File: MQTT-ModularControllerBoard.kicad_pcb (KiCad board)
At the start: 4 copper layers, 200 x 45 mm, 83 parts, among them IC301 LM74700QDBVTQ1, IC401 TLV76733DRVR, IC403 LM74700QDBVTQ1, J301 1715721, J501 A2541HWV-10P, J502 A2541HWV-10P, J503 A2541HWV-10P, J504 A2541HWV-10P, J505 A2541HWV-10P, J506 A2541HWV-10P, J507 A2541HWV-10P, J508 A2541HWV-10P, J601 1051640001, Q301 60V 38A, Q402 60V 38A, U201 ESP32-S3-WROOM-1U-N16R8, U601 ESD Protection IC

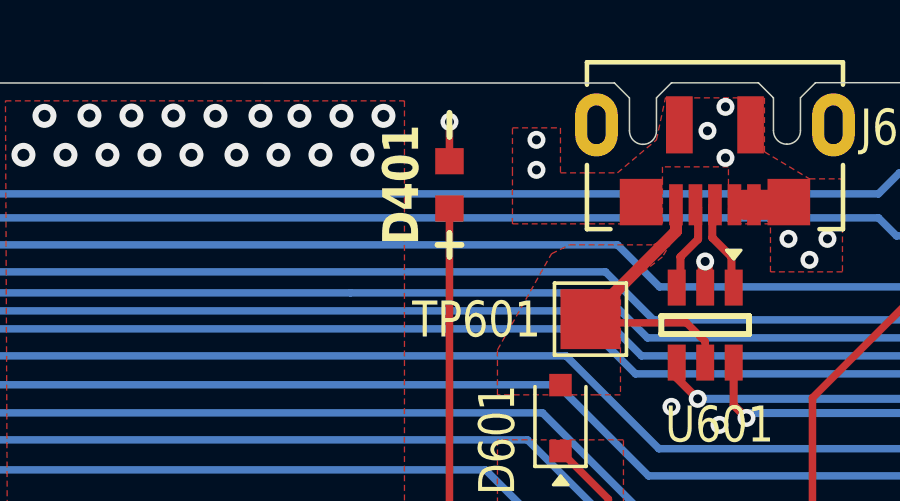
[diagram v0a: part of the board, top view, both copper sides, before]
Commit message: Silkscreen Updates and BOM added
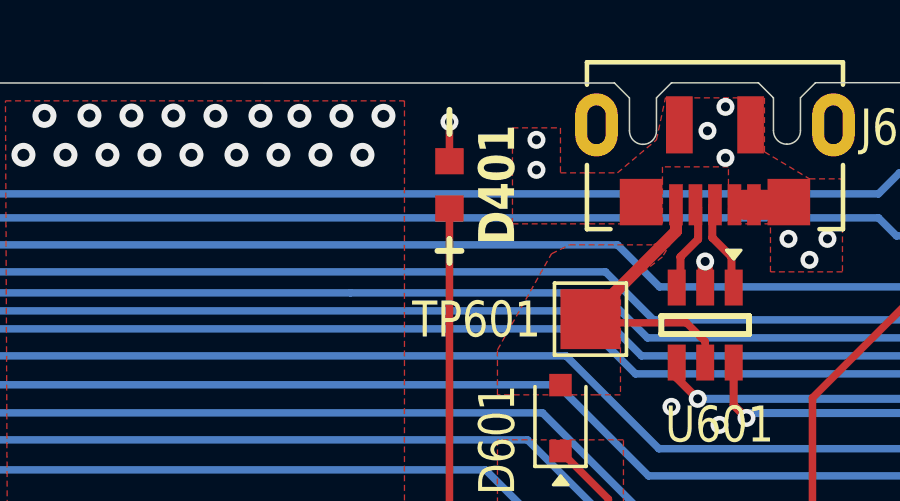
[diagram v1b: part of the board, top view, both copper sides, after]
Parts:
- turned D401 to 90 degrees
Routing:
- net Net-(D401-A): track 20.7 -> 22.0 mm
- net GND: track 78.1 -> 76.8 mm
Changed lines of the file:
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@@
 	(footprint "JLCPCB Basic:LED_0603_1608Metric"
 		(layer "F.Cu")
-		(at 171.5 94.9 -90)
+		(at 171.5 94.9 90)
 		(descr "LED SMD 0603 (1608 Metric), square (rectangular) end terminal, IPC-7351 nominal, (Body size source: http://www.tortai-tech.com/upload/download/2011102023233369053.pdf), generated with kicad-footprint-generator")
 		(tags "LED")
 		(property "Reference" "D401"
-			(at 0 1.6 270)
+			(at 0 1.6 90)
 			(layer "F.SilkS")
 			(effects
@@
 		)
 		(property "Value" "KT-0603R"
-			(at 4.1 7.4 180)
+			(at 4.1 7.4 0)
 			(layer "F.Fab")
 			(hide yes)
@@
 		)
 		(property "Sim.Pins" "1=K 2=A"
-			(at 0 0 270)
+			(at 0 0 90)
 			(unlocked yes)
 			(layer "F.Fab")
@@
 		)
 		(property "Manufacturer" "Hubei KENTO Elec"
-			(at 0 0 270)
+			(at 0 0 90)
 			(unlocked yes)
 			(layer "F.Fab")
@@
 		)
 		(property "Manufacturer Part No" " KT-0603R"
-			(at 0 0 270)
+			(at 0 0 90)
 			(unlocked yes)
 			(layer "F.Fab")
@@
 		)
 		(property "JLCPCB Part #" "C2286"
-			(at 0 0 270)
+			(at 0 0 90)
 			(unlocked yes)
 			(layer "F.Fab")
@@
 		)
 		(property "Package" "0603"
-			(at 0 0 270)
+			(at 0 0 90)
 			(unlocked yes)
 			(layer "F.Fab")
@@
 		)
 		(property "Part Type" "Basic"
-			(at 0 0 270)
+			(at 0 0 90)
 			(unlocked yes)
 			(layer "F.Fab")
@@
 		(attr smd)
 		(fp_line
-			(start -2.4 0)
-			(end -1.6 0)
+			(start -2.2 -0.4)
+			(end -2.2 0.4)
 			(stroke
 				(width 0.2)
@@
 		)
 		(fp_line
-			(start 1.6 0)
-			(end 2.4 0)
+			(start 1.7 0)
+			(end 2.5 0)
 			(stroke
 				(width 0.2)
@@
 		)
 		(fp_line
-			(start 2 -0.4)
-			(end 2 0.4)
+			(start -2.6 0)
+			(end -1.8 0)
 			(stroke
 				(width 0.2)
@@
 		)
 		(fp_line
-			(start -1.48 0.73)
-			(end -1.48 -0.73)
+			(start 1.48 -0.73)
+			(end 1.48 0.73)
 			(stroke
 				(width 0.05)
@@
 		)
 		(fp_line
-			(start 1.48 0.73)
-			(end -1.48 0.73)
+			(start -1.48 -0.73)
+			(end 1.48 -0.73)
 			(stroke
 				(width 0.05)
@@
 		)
 		(fp_line
-			(start -1.48 -0.73)
-			(end 1.48 -0.73)
+			(start 1.48 0.73)
+			(end -1.48 0.73)
 			(stroke
 				(width 0.05)
@@
 		)
 		(fp_line
-			(start 1.48 -0.73)
-			(end 1.48 0.73)
+			(start -1.48 0.73)
+			(end -1.48 -0.73)
 			(stroke
 				(width 0.05)
@@
 		)
 		(fp_line
-			(start -0.8 0.4)
-			(end 0.8 0.4)
+			(start 0.8 -0.4)
+			(end -0.8 -0.4)
 			(stroke
 				(width 0.1)
@@
 		)
 		(fp_line
-			(start 0.8 0.4)
-			(end 0.8 -0.4)
+			(start -0.8 -0.4)
+			(end -0.8 0.4)
 			(stroke
 				(width 0.1)
@@
 		)
 		(fp_line
-			(start 0.1 0.25)
-			(end -0.2 0)
+			(start 0.1 -0.25)
+			(end 0.1 0.25)
 			(stroke
 				(width 0.1)
@@
 		)
 		(fp_line
-			(start -0.2 0)
-			(end -0.4 0)
+			(start -0.2 -0.25)
+			(end -0.2 0.25)
 			(stroke
 				(width 0.1)
@@
 		)
 		(fp_line
-			(start -0.2 0)
-			(end 0.1 -0.25)
+			(start 0.1 0)
+			(end 0.3 0)
 			(stroke
 				(width 0.1)
@@
 		)
 		(fp_line
-			(start 0.1 0)
-			(end 0.3 0)
+			(start -0.2 0)
+			(end 0.1 -0.25)
 			(stroke
 				(width 0.1)
@@
 		)
 		(fp_line
-			(start -0.2 -0.25)
-			(end -0.2 0.25)
+			(start -0.2 0)
+			(end -0.4 0)
 			(stroke
 				(width 0.1)
@@
 		)
 		(fp_line
-			(start 0.1 -0.25)
-			(end 0.1 0.25)
+			(start 0.1 0.25)
+			(end -0.2 0)
 			(stroke
 				(width 0.1)
@@
 		)
 		(fp_line
-			(start -0.8 -0.4)
-			(end -0.8 0.4)
+			(start 0.8 0.4)
+			(end 0.8 -0.4)
 			(stroke
 				(width 0.1)
@@
 		)
 		(fp_line
-			(start 0.8 -0.4)
-			(end -0.8 -0.4)
+			(start -0.8 0.4)
+			(end 0.8 0.4)
 			(stroke
 				(width 0.1)
@@
 		)
 		(fp_text user "${REFERENCE}"
-			(at 0 3.1 180)
+			(at 0 3.1 0)
 			(layer "F.Fab")
 			(effects
@@
 		)
 		(pad "1" smd rect
-			(at -0.7875 0 270)
+			(at -0.7875 0 90)
 			(size 0.875 0.95)
 			(layers "F.Cu" "F.Mask" "F.Paste")
@@
 		)
 		(pad "2" smd rect
-			(at 0.7875 0 270)
+			(at 0.7875 0 90)
 			(size 0.875 0.95)
 			(layers "F.Cu" "F.Mask" "F.Paste")
@@
 	)
 	(segment
-		(start 171.5 92.8)
-		(end 171.5 94.1125)
-		(width 0.25)
-		(layer "F.Cu")
-		(net 2)
-	)
-	(segment
 		(start 198.8 93.1)
 		(end 199.9 94.2)
@@
 		(width 0.25)
 		(layer "F.Cu")
+		(net 17)
+	)
+	(segment
+		(start 171.5 92.8)
+		(end 171.5 94.1125)
+		(width 0.25)
+		(layer "F.Cu")
